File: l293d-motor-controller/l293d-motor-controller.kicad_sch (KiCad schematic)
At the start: 13 parts, among them M1 Motor_DC, M2 Motor_DC, U1 LM7805, U2 L293D, U3 74HC04

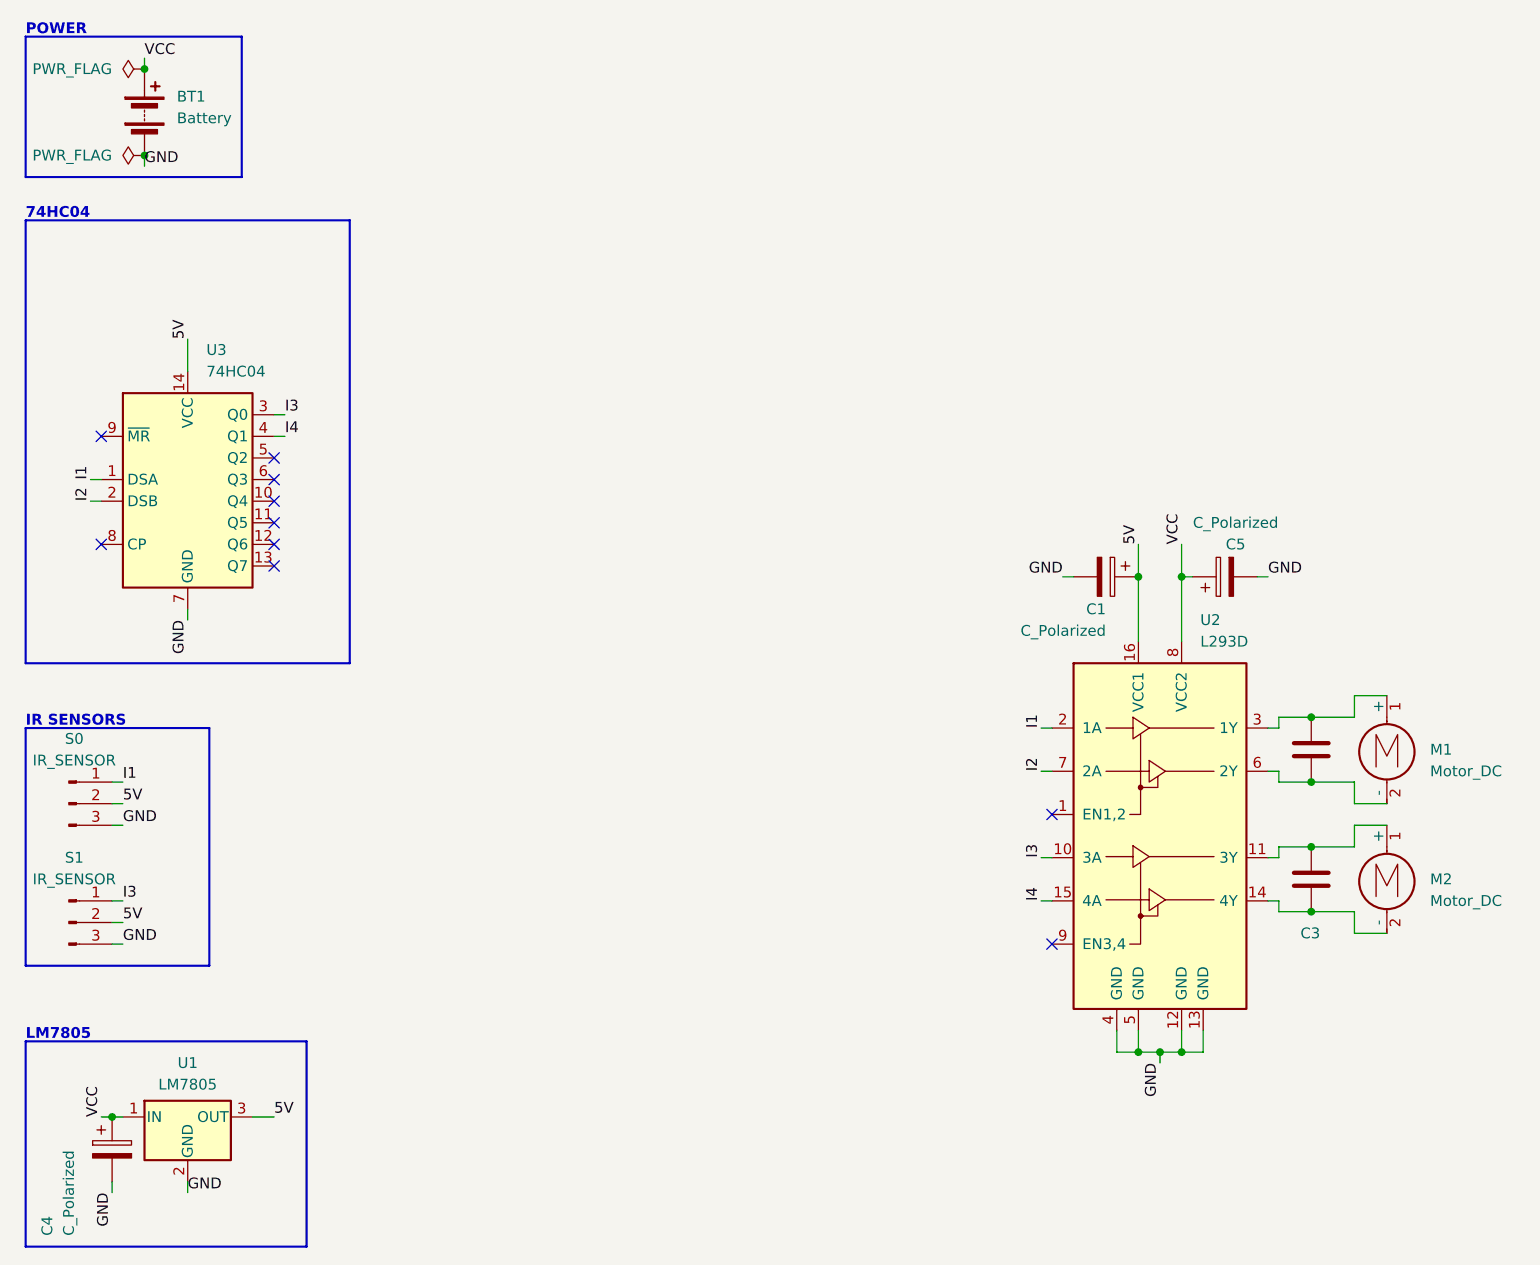
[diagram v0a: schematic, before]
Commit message: project 3 / l293d motor driver / design improved
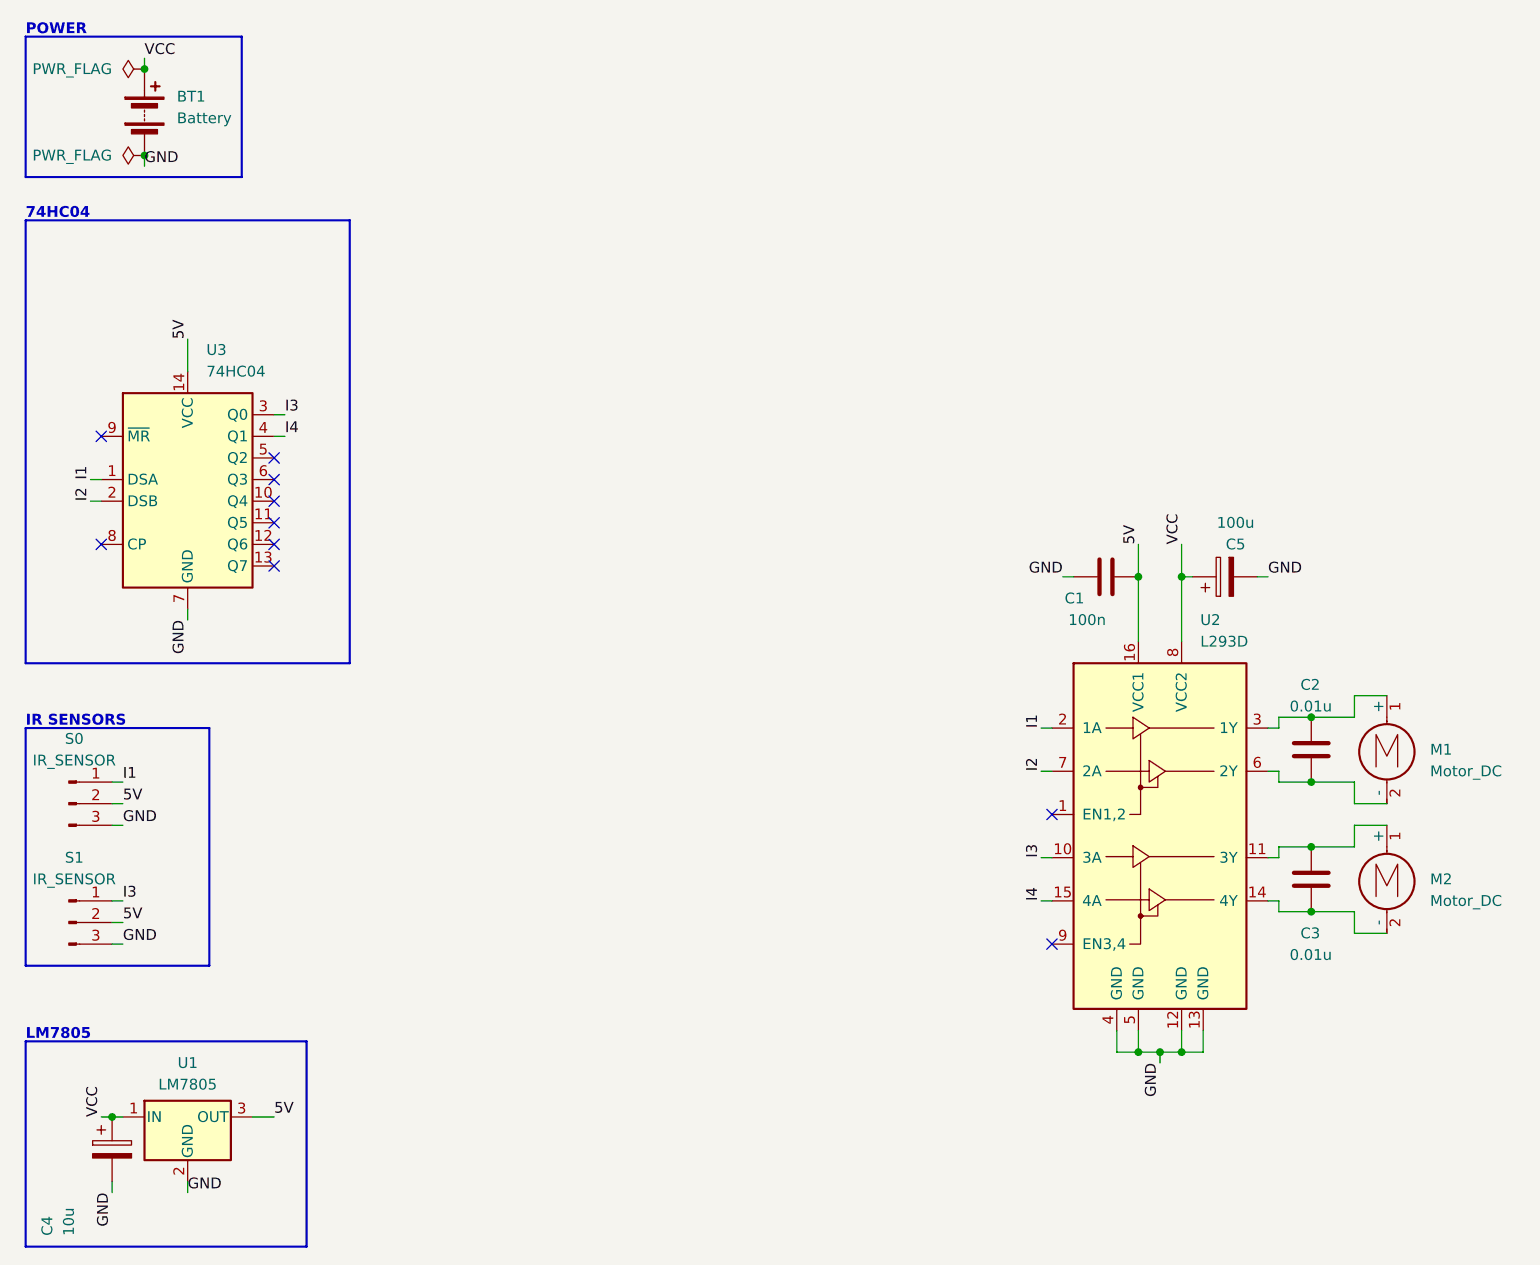
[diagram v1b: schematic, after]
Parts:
- removed C1: C_Polarized, Capacitor_THT:CP_Radial_D4.0mm_P1.50mm, symbol Device:C_Polarized
- added C1: 100n, Capacitor_THT:C_Disc_D3.0mm_W1.6mm_P2.50mm, symbol Device:C
- C2, C3: value C -> 0.01u
- C4: value C_Polarized -> 10u
- C5: value C_Polarized -> 100u
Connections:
- net 5V: now also C1.2
- net GND: now also C1.1
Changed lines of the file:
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@@
   (junction (at 147.32 137.16) (diameter 0) (color 0 0 0 0)
   )
+  (junction (at 147.32 81.28) (diameter 0) (color 0 0 0 0)
+  )
   (junction (at 167.64 120.65) (diameter 0) (color 0 0 0 0)
   )
   (junction (at 152.4 137.16) (diameter 0) (color 0 0 0 0)
-  )
-  (junction (at 147.32 81.28) (diameter 0) (color 0 0 0 0)
   )
   (junction (at 167.64 97.79) (diameter 0) (color 0 0 0 0)
@@
     (stroke (width 0) (type default))
   )
+  (wire (pts (xy 147.32 77.47) (xy 147.32 81.28))
+    (stroke (width 0) (type default))
+  )
+  (wire (pts (xy 135.89 119.38) (xy 137.16 119.38))
+    (stroke (width 0) (type default))
+  )
+  (wire (pts (xy 154.94 137.16) (xy 154.94 134.62))
+    (stroke (width 0) (type default))
+  )
+  (wire (pts (xy 163.83 120.65) (xy 163.83 119.38))
+    (stroke (width 0) (type default))
+  )
+  (wire (pts (xy 163.83 105.41) (xy 167.64 105.41))
+    (stroke (width 0) (type default))
+  )
+  (wire (pts (xy 26.67 110.49) (xy 27.94 110.49))
+    (stroke (width 0) (type default))
+  )
+  (wire (pts (xy 26.67 152.4) (xy 26.67 153.67))
+    (stroke (width 0) (type default))
+  )
+  (wire (pts (xy 26.67 119.38) (xy 27.94 119.38))
+    (stroke (width 0) (type default))
+  )
+  (wire (pts (xy 144.78 137.16) (xy 144.78 134.62))
+    (stroke (width 0) (type default))
+  )
+  (wire (pts (xy 172.72 113.03) (xy 172.72 110.49))
+    (stroke (width 0) (type default))
+  )
+  (wire (pts (xy 172.72 123.19) (xy 176.53 123.19))
+    (stroke (width 0) (type default))
+  )
+  (wire (pts (xy 26.67 107.95) (xy 27.94 107.95))
+    (stroke (width 0) (type default))
+  )
+  (wire (pts (xy 147.32 137.16) (xy 149.86 137.16))
+    (stroke (width 0) (type default))
+  )
+  (wire (pts (xy 24.13 72.39) (xy 25.4 72.39))
+    (stroke (width 0) (type default))
+  )
+  (wire (pts (xy 152.4 81.28) (xy 152.4 88.9))
+    (stroke (width 0) (type default))
+  )
+  (wire (pts (xy 35.56 152.4) (xy 35.56 153.67))
+    (stroke (width 0) (type default))
+  )
+  (wire (pts (xy 163.83 114.3) (xy 162.56 114.3))
+    (stroke (width 0) (type default))
+  )
+  (wire (pts (xy 172.72 97.79) (xy 172.72 95.25))
+    (stroke (width 0) (type default))
+  )
+  (wire (pts (xy 43.18 144.78) (xy 45.72 144.78))
+    (stroke (width 0) (type default))
+  )
+  (wire (pts (xy 135.89 104.14) (xy 137.16 104.14))
+    (stroke (width 0) (type default))
+  )
+  (wire (pts (xy 138.43 81.28) (xy 139.7 81.28))
+    (stroke (width 0) (type default))
+  )
+  (wire (pts (xy 162.56 81.28) (xy 161.29 81.28))
+    (stroke (width 0) (type default))
+  )
+  (wire (pts (xy 163.83 120.65) (xy 167.64 120.65))
+    (stroke (width 0) (type default))
+  )
   (wire (pts (xy 147.32 81.28) (xy 147.32 88.9))
-    (stroke (width 0) (type default))
-  )
-  (wire (pts (xy 135.89 119.38) (xy 137.16 119.38))
-    (stroke (width 0) (type default))
-  )
-  (wire (pts (xy 154.94 137.16) (xy 154.94 134.62))
-    (stroke (width 0) (type default))
-  )
-  (wire (pts (xy 163.83 120.65) (xy 163.83 119.38))
-    (stroke (width 0) (type default))
-  )
-  (wire (pts (xy 163.83 105.41) (xy 167.64 105.41))
-    (stroke (width 0) (type default))
-  )
-  (wire (pts (xy 26.67 110.49) (xy 27.94 110.49))
-    (stroke (width 0) (type default))
-  )
-  (wire (pts (xy 26.67 152.4) (xy 26.67 153.67))
-    (stroke (width 0) (type default))
-  )
-  (wire (pts (xy 26.67 119.38) (xy 27.94 119.38))
-    (stroke (width 0) (type default))
-  )
-  (wire (pts (xy 144.78 137.16) (xy 144.78 134.62))
-    (stroke (width 0) (type default))
-  )
-  (wire (pts (xy 172.72 113.03) (xy 172.72 110.49))
-    (stroke (width 0) (type default))
-  )
-  (wire (pts (xy 172.72 123.19) (xy 176.53 123.19))
-    (stroke (width 0) (type default))
-  )
-  (wire (pts (xy 26.67 107.95) (xy 27.94 107.95))
-    (stroke (width 0) (type default))
-  )
-  (wire (pts (xy 147.32 137.16) (xy 149.86 137.16))
-    (stroke (width 0) (type default))
-  )
-  (wire (pts (xy 24.13 72.39) (xy 25.4 72.39))
-    (stroke (width 0) (type default))
-  )
-  (wire (pts (xy 152.4 81.28) (xy 152.4 88.9))
-    (stroke (width 0) (type default))
-  )
-  (wire (pts (xy 35.56 152.4) (xy 35.56 153.67))
-    (stroke (width 0) (type default))
-  )
-  (wire (pts (xy 163.83 114.3) (xy 162.56 114.3))
-    (stroke (width 0) (type default))
-  )
-  (wire (pts (xy 172.72 97.79) (xy 172.72 95.25))
-    (stroke (width 0) (type default))
-  )
-  (wire (pts (xy 43.18 144.78) (xy 45.72 144.78))
-    (stroke (width 0) (type default))
-  )
-  (wire (pts (xy 135.89 104.14) (xy 137.16 104.14))
-    (stroke (width 0) (type default))
-  )
-  (wire (pts (xy 138.43 81.28) (xy 139.7 81.28))
-    (stroke (width 0) (type default))
-  )
-  (wire (pts (xy 162.56 81.28) (xy 161.29 81.28))
-    (stroke (width 0) (type default))
-  )
-  (wire (pts (xy 163.83 120.65) (xy 167.64 120.65))
-    (stroke (width 0) (type default))
-  )
-  (wire (pts (xy 147.32 77.47) (xy 147.32 81.28))
     (stroke (width 0) (type default))
   )
@@
       (effects (font (size 1.27 1.27)) (justify left))
     )
-    (property "Value" "C" (at 171.45 120.65 0)
-      (effects (font (size 1.27 1.27)) (justify left) hide)
+    (property "Value" "0.01u" (at 165.1 125.73 0)
+      (effects (font (size 1.27 1.27)) (justify left))
     )
     (property "Footprint" "Capacitor_THT:C_Disc_D3.0mm_W1.6mm_P2.50mm" (at 168.6052 120.65 0)
@@
       (effects (font (size 1.27 1.27)))
     )
-    (property "Value" "C_Polarized" (at 158.75 74.93 90)
+    (property "Value" "100u" (at 158.75 74.93 90)
       (effects (font (size 1.27 1.27)))
     )
@@
         (path "/a47e20e4-3b17-4b26-83db-a8287d7077d8"
           (reference "C5") (unit 1)
+        )
+      )
+    )
+  )
+  (symbol (lib_id "Device:C") (at 143.51 81.28 90) (unit 1)
+    (in_bom yes) (on_board yes) (dnp no)
+    (property "Reference" "C1" (at 140.97 83.82 90)
+      (effects (font (size 1.27 1.27)) (justify left))
+    )
+    (property "Value" "100n" (at 143.51 86.36 90)
+      (effects (font (size 1.27 1.27)) (justify left))
+    )
+    (property "Footprint" "Capacitor_THT:C_Disc_D3.0mm_W1.6mm_P2.50mm" (at 147.32 80.3148 0)
+      (effects (font (size 1.27 1.27)) hide)
+    )
+    (property "Datasheet" "~" (at 143.51 81.28 0)
+      (effects (font (size 1.27 1.27)) hide)
+    )
+    (pin "1")
+    (pin "2")
+    (instances
+      (project "l293d-motor-controller"
+        (path "/a47e20e4-3b17-4b26-83db-a8287d7077d8"
+          (reference "C1") (unit 1)
         )
       )
@@
   )
   (symbol (lib_id "Device:C") (at 167.64 101.6 0) (unit 1)
-    (in_bom yes) (on_board yes) (dnp no) (fields_autoplaced)
-    (property "Reference" "C2" (at 171.45 100.33 0)
-      (effects (font (size 1.27 1.27)) (justify left) hide)
-    )
-    (property "Value" "C" (at 171.45 102.87 0)
-      (effects (font (size 1.27 1.27)) (justify left) hide)
+    (in_bom yes) (on_board yes) (dnp no)
+    (property "Reference" "C2" (at 166.37 93.98 0)
+      (effects (font (size 1.27 1.27)) (justify left))
+    )
+    (property "Value" "0.01u" (at 165.1 96.52 0)
+      (effects (font (size 1.27 1.27)) (justify left))
     )
     (property "Footprint" "Capacitor_THT:C_Disc_D3.0mm_W1.6mm_P2.50mm" (at 168.6052 105.41 0)
@@
     )
   )
-  (symbol (lib_id "Device:C_Polarized") (at 143.51 81.28 270) (unit 1)
-    (in_bom yes) (on_board yes) (dnp no)
-    (property "Reference" "C1" (at 143.51 85.09 90)
-      (effects (font (size 1.27 1.27)) (justify right))
-    )
-    (property "Value" "C_Polarized" (at 143.51 87.63 90)
-      (effects (font (size 1.27 1.27)) (justify right))
-    )
-    (property "Footprint" "Capacitor_THT:CP_Radial_D4.0mm_P1.50mm" (at 139.7 82.2452 0)
-      (effects (font (size 1.27 1.27)) hide)
-    )
-    (property "Datasheet" "~" (at 143.51 81.28 0)
-      (effects (font (size 1.27 1.27)) hide)
-    )
-    (pin "1")
-    (pin "2")
-    (instances
-      (project "l293d-motor-controller"
-        (path "/a47e20e4-3b17-4b26-83db-a8287d7077d8"
-          (reference "C1") (unit 1)
-        )
-      )
-    )
-  )
   (symbol (lib_id "Device:C_Polarized") (at 26.67 148.59 0) (unit 1)
     (in_bom yes) (on_board yes) (dnp no)
@@
       (effects (font (size 1.27 1.27)) (justify left))
     )
-    (property "Value" "C_Polarized" (at 21.59 158.75 90)
-      (effects (font (size 1.27 1.27)) (justify left))
-    )
+    (property "Value" "10u" (at 21.59 158.75 90)
+      (effects (font (size 1.27 1.27)) (justify left))
+    )

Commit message: project 3 / l293d motor driver / layout improvement
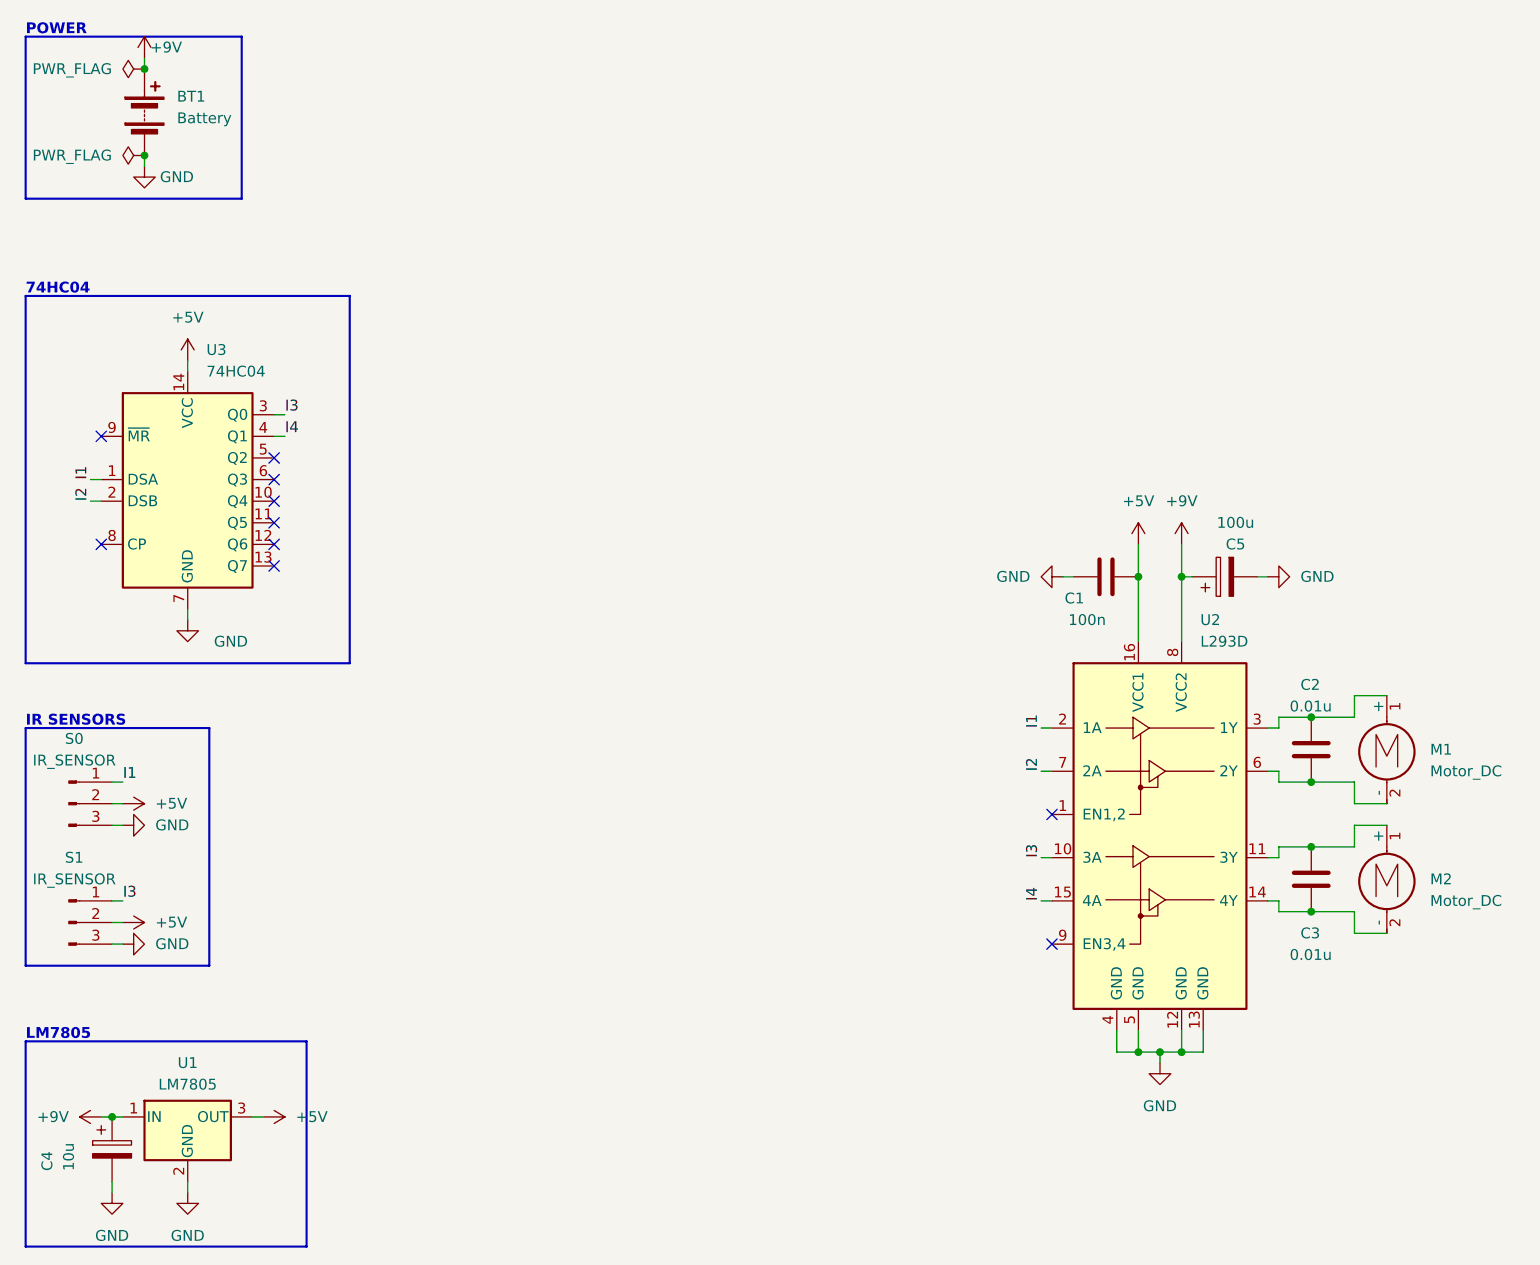
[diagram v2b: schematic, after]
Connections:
- net 5V renamed +5V
- net VCC renamed +9V
